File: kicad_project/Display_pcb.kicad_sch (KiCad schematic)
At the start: 14 parts, among them J3 USB C, J8 33FXRH-SM1-GAN-TF, U16 USBLC6-2SC6

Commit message: Pcb to production
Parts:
- removed R19, R20, R21: 0R, Resistor_SMD:R_0402_1005Metric, symbol Device:R
- removed R22: TBD, Resistor_SMD:R_0402_1005Metric, symbol Device:R
- added NT1, NT2: NetTie_2, NetTie:NetTie-2_SMD_Pad0.5mm, symbol Device:NetTie_2
- added U6: DO0200FS01, symbol Display:DO0200FS01
- AE1: now left out of the parts list
- J3: footprint hwlab:USB_C_Receptacle_HCTL_HC019-1E1H1A103-0HR -> paltatech:USB_C_Receptacle_HCTL_HC019-1E1H1A103-0HR
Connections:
- net EAVDD is gone; now on net GND: J8.7 (Pin_7)
- net +3V3: now also NT1.2, NT2.2; no longer C32.1, C33.1
- net 4.6V: now also J8.3 (Pin_3), J8.4 (Pin_4); no longer J8.30 (Pin_30), J8.31 (Pin_31)
- net GND: now also J8.1 (Pin_1), J8.2 (Pin_2)
- net OL_D0: now also J8.20 (Pin_20); no longer J8.14 (Pin_14)
- net OL_D1: now also J8.19 (Pin_19); no longer J8.15 (Pin_15)
- net OL_D2: now also J8.16 (Pin_16); no longer J8.18 (Pin_18)
- net OL_D3: now also J8.15 (Pin_15); no longer J8.19 (Pin_19)
- net OL_RESET: now also J8.22 (Pin_22); no longer J8.12 (Pin_12)
- net OL_SCK: now also J8.18 (Pin_18); no longer J8.16 (Pin_16)
- net OL_SD0: now also J8.21 (Pin_21); no longer J8.13 (Pin_13)
- net OL_TE: now also J8.23 (Pin_23); no longer J8.11 (Pin_11)
- net -2V2: no longer names the net of J8.32 (Pin_32)
- net -2V2: no longer J8.33 (Pin_33)
- net IM0 renamed AVDD
- net AVDD: now also C32.1, NT1.1
- net IM1: no longer names the net of J8.26 (Pin_26)
- net IM1: now also C33.1, NT2.1
- net OL_EN: no longer names the net of J8.10 (Pin_10)
- net SWIRE: no longer names the net of J8.9 (Pin_9)
- no-connect marks 40 -> 42
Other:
- sheet POWER ports: added DISPLAY_PWR_EN; removed OL_EN, SWIRE
- note added: "IM0=0, IM1=0 -> 3-WIRE SPI IM0=0, IM1=1 -> 4-WIRE SPI (USE here) IM0=1, IM1=0 -> QSPI IM0=1, IM1=1 -> I8080- 8 BIT"
- moved on the sheet: AE1, C32, C33, J3, J8, R5, R6, TP1, TP5, U16

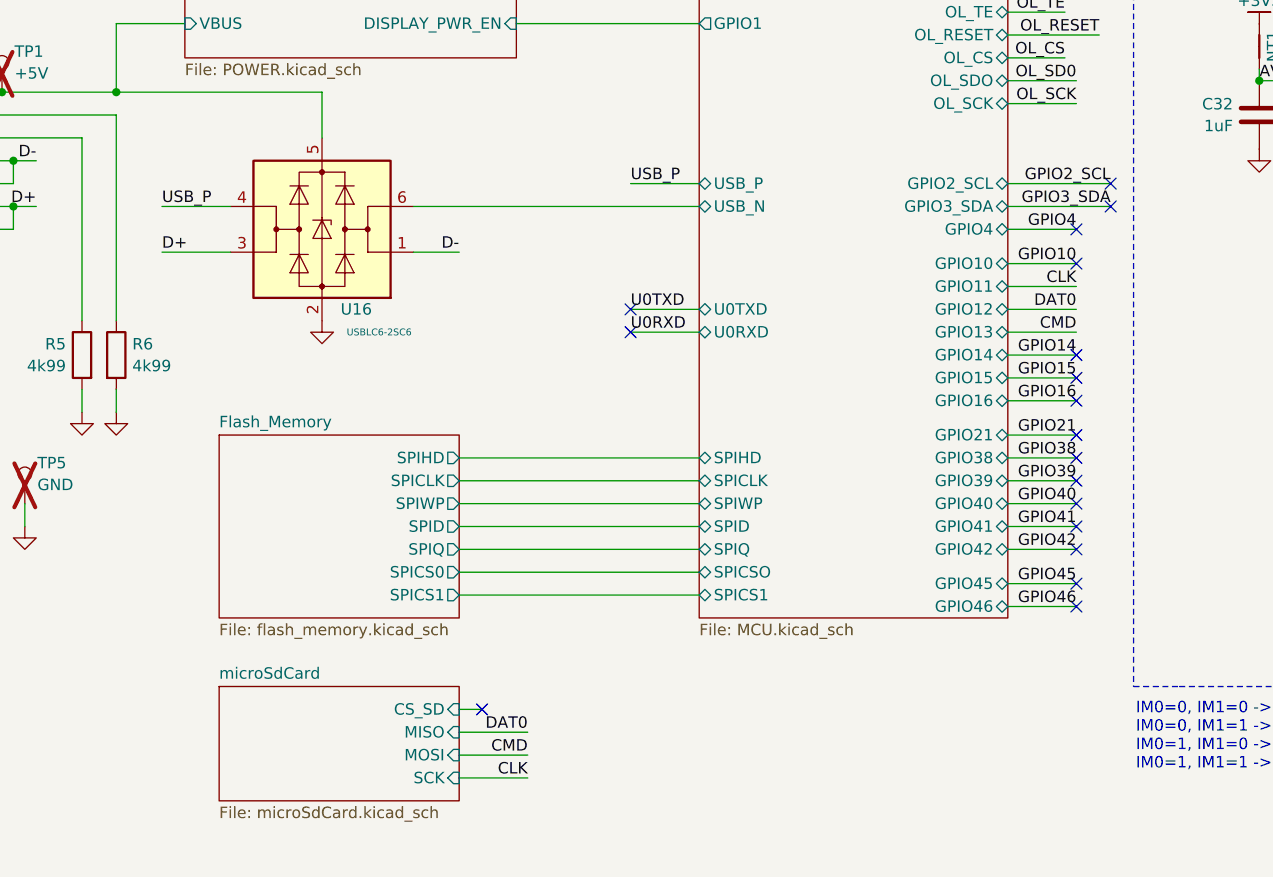
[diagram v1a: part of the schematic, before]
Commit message: Design revision: SD improvements, flash update, silkscreen and USB differential fix
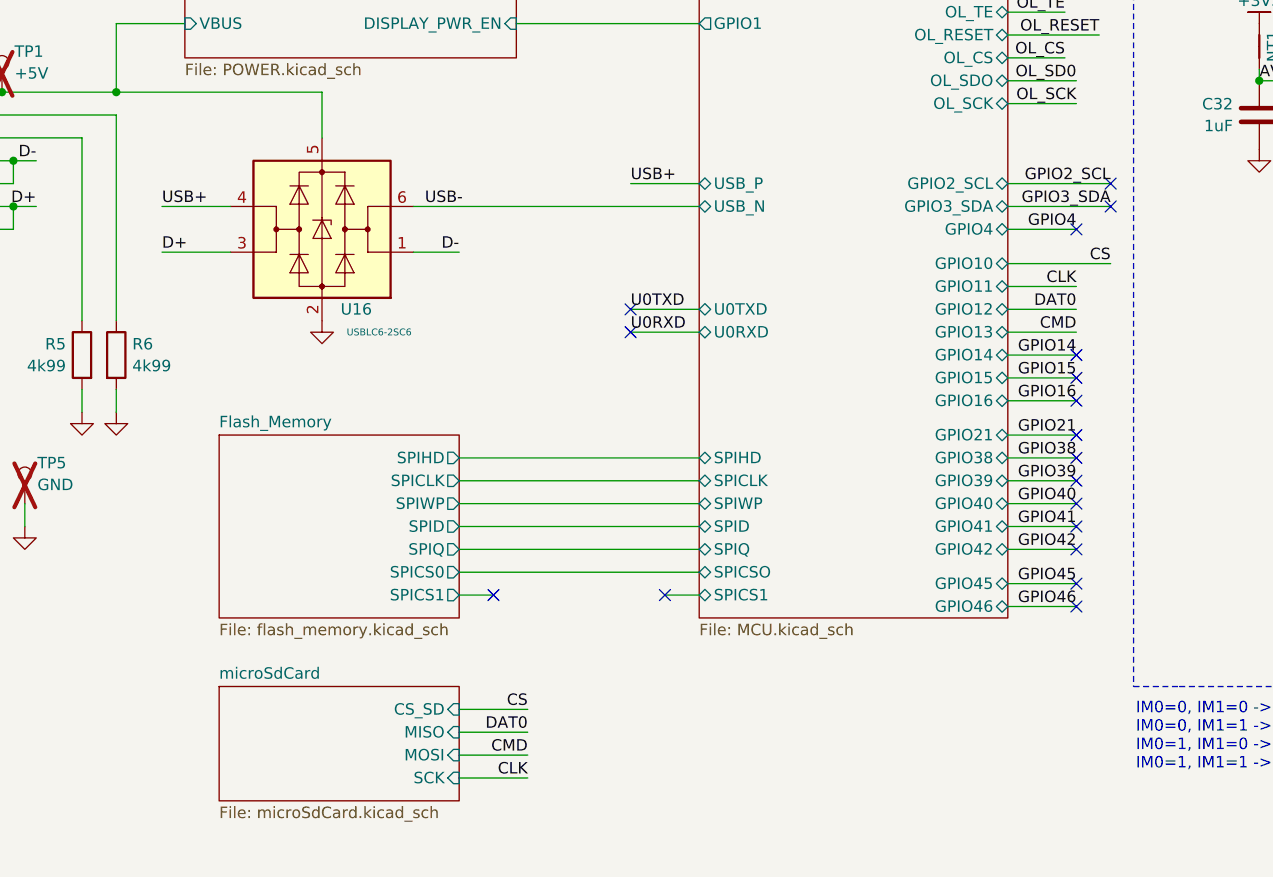
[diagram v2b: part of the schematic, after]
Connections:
- net MCU/USB_N renamed USB-
- net USB_P renamed USB+
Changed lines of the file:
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@@
-	)
-	(no_connect
-		(at 101.6 148.59)
 	)
 	(no_connect
@@
 	)
 	(no_connect
+		(at 102.87 135.89)
+	)
+	(no_connect
 		(at 46.99 97.79)
 	)
@@
 	)
 	(no_connect
-		(at 167.64 99.06)
-	)
-	(no_connect
 		(at 171.45 90.17)
 	)
@@
 	)
 	(no_connect
+		(at 121.92 135.89)
+	)
+	(no_connect
 		(at 213.36 118.11)
 	)
@@
 	(wire
 		(pts
-			(xy 160.02 99.06) (xy 167.64 99.06)
+			(xy 160.02 99.06) (xy 171.45 99.06)
 		)
 		(stroke
@@
 	(wire
 		(pts
-			(xy 99.06 148.59) (xy 101.6 148.59)
+			(xy 99.06 148.59) (xy 106.68 148.59)
 		)
 		(stroke
@@
 	(wire
 		(pts
+			(xy 99.06 135.89) (xy 102.87 135.89)
+		)
+		(stroke
+			(width 0)
+			(type default)
+		)
+	)
+	(wire
+		(pts
 			(xy 160.02 104.14) (xy 167.64 104.14)
 		)
@@
 	(wire
 		(pts
-			(xy 99.06 135.89) (xy 125.73 135.89)
-		)
-		(stroke
-			(width 0)
-			(type default)
-		)
-	)
-	(wire
-		(pts
 			(xy 160.02 123.19) (xy 167.64 123.19)
 		)
@@
 		(pts
 			(xy 160.02 137.16) (xy 167.64 137.16)
+		)
+		(stroke
+			(width 0)
+			(type default)
+		)
+	)
+	(wire
+		(pts
+			(xy 121.92 135.89) (xy 125.73 135.89)
 		)
 		(stroke
@@
 		)
 	)
+	(label "CS"
+		(at 171.45 99.06 180)
+		(effects
+			(font
+				(size 1.27 1.27)
+			)
+			(justify right bottom)
+		)
+	)
 	(label "AVDD"
 		(at 207.01 74.93 0)
@@
 		)
 	)
+	(label "USB-"
+		(at 95.25 92.71 0)
+		(effects
+			(font
+				(size 1.27 1.27)
+			)
+			(justify left bottom)
+		)
+	)
 	(label "OL_TE"
 		(at 166.37 71.12 180)
@@
 		)
 	)
-	(label "USB_P"
+	(label "USB+"
 		(at 66.04 92.71 0)
 		(effects
@@
 		)
 	)
+	(label "CS"
+		(at 106.68 148.59 180)
+		(effects
+			(font
+				(size 1.27 1.27)
+			)
+			(justify right bottom)
+		)
+	)
 	(label "OL_SD0"
 		(at 204.47 90.17 0)
@@
 		)
 	)
-	(label "USB_P"
+	(label "USB+"
 		(at 118.11 90.17 0)
 		(effects
@@
 		)
 	)
-	(label "GPIO10"
-		(at 167.64 99.06 180)
-		(effects
-			(font
-				(size 1.27 1.27)
-			)
-			(justify right bottom)
-		)
-	)
